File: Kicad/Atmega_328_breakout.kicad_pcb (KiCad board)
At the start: 2 copper layers, 73.8 x 62 mm, 83 parts, among them J1 Power_connector, J10 Device_Connector, J11 Power terminal, J12 Jack-DC, J13 1x2, J14 1x2, J15 1x2, J16 1x2, J17 Conn_01x06, J18 1x2, J19 1x2, J2 ADC_Connector, J20 1x2, J21 1x2, J22 1x2, J23 1x2, J24 1x2, J25 1x2, J26 1x2, J27 1x2, J28 1x2, J29 1x2, J3 Com_header, J30 Pin out, J4 PORB++_connector, J5 PORD_connector, J6 USB, J7 Conn_01x01, Q1 PMOS, SW1 SW_Push, SW2 SW_Push, U1 MCP1700-33, U2 TL071, U3 ATMEGA328P-AU, U4 L7805, U5 MCP2221, U6 NCP1117-5, Y1 Crystal

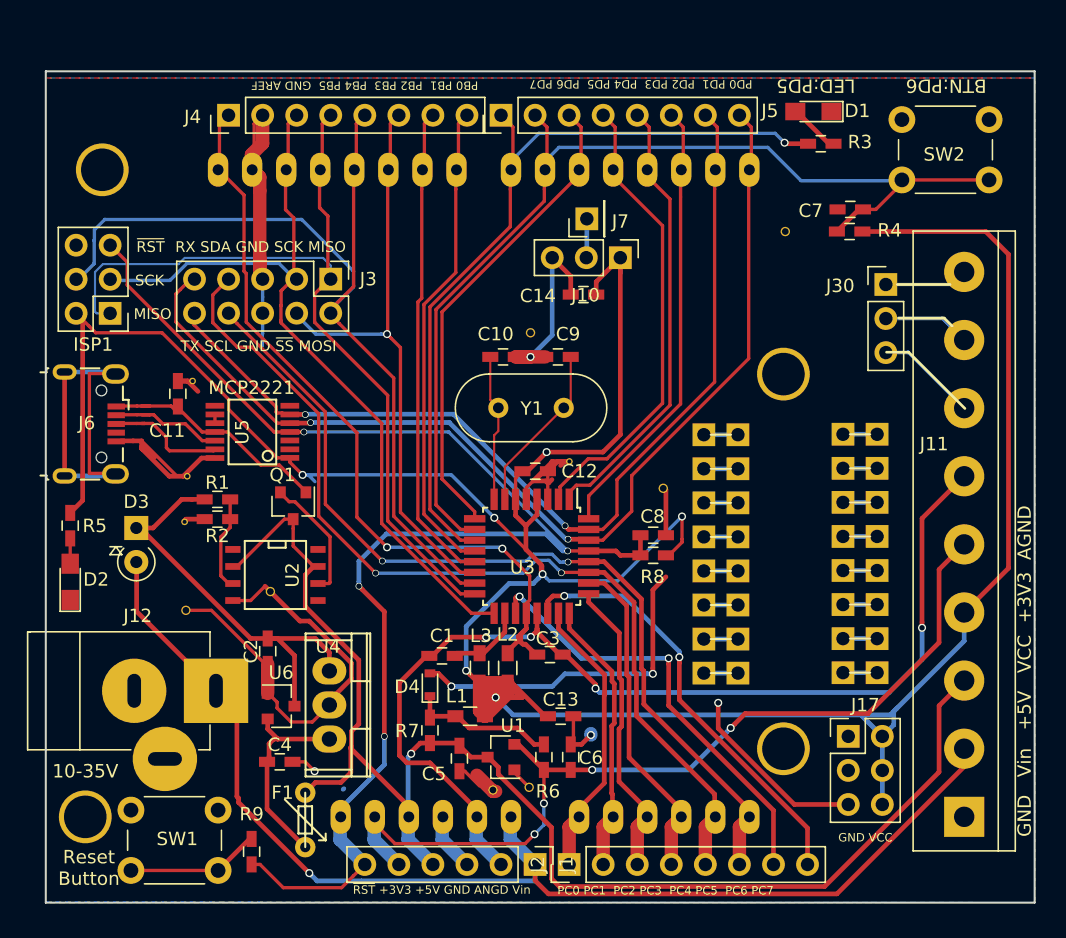
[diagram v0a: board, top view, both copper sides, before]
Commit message: fixed it for kicad 5
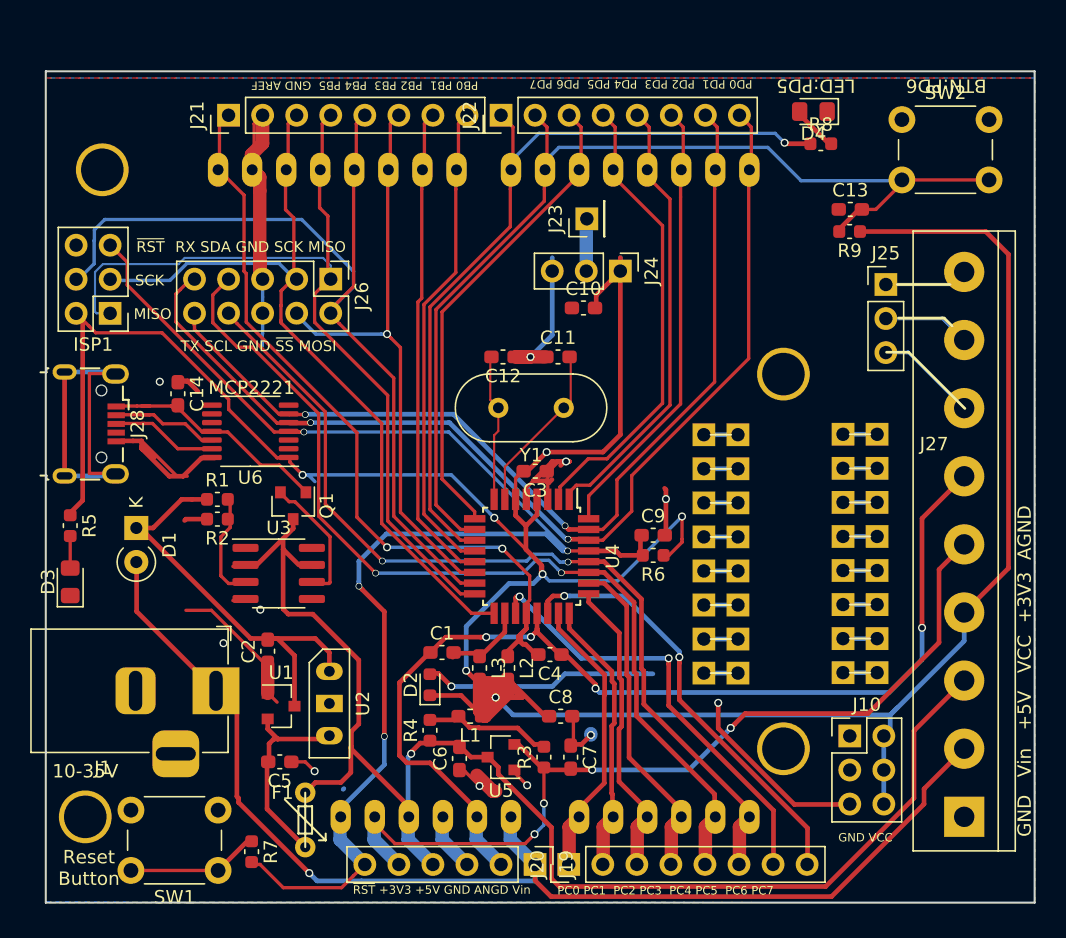
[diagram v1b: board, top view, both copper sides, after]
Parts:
- removed G***: LOGO, jorgen:LOGO
- removed GND (x6), REF**: VIA_GND, jorgen:VIA_GND_0,5
- removed GND (x3), REF**: VIA_GND, jorgen:VIA_GND_0,3
- removed the J17 at (110.1, 103.6)
- removed the J2 at (89.3, 113.2)
- removed the R7 at (78.9, 103.2)
- added J10: Conn_01x06, Connector_PinHeader_2.54mm:PinHeader_2x03_P2.54mm_Vertical, F.Cu at (110.2, 103.6)
- added J20: ADC_Connector, Connector_PinHeader_2.54mm:PinHeader_1x08_P2.54mm_Vertical, F.Cu at (89.2, 113.2)
- added R4: 0R, Capacitor_SMD:C_0603_1608Metric, F.Cu at (78.9, 103.2)
- C1, C2: footprint Capacitors_SMD:C_0603_HandSoldering -> Capacitor_SMD:C_0603_1608Metric_Pad1.08x0.95mm_HandSolder
- C10: renamed from C14; footprint Capacitors_SMD:C_0603_HandSoldering -> Capacitor_SMD:C_0603_1608Metric_Pad1.08x0.95mm_HandSolder
- C11: renamed from C9; footprint Capacitors_SMD:C_0603_HandSoldering -> Capacitor_SMD:C_0603_1608Metric_Pad1.08x0.95mm_HandSolder
- C12: renamed from C10; footprint Capacitors_SMD:C_0603_HandSoldering -> Capacitor_SMD:C_0603_1608Metric_Pad1.08x0.95mm_HandSolder
- C13: renamed from C7; footprint Capacitors_SMD:C_0603_HandSoldering -> Capacitor_SMD:C_0603_1608Metric_Pad1.08x0.95mm_HandSolder
- C14: renamed from C11; footprint Capacitors_SMD:C_0603_HandSoldering -> Capacitor_SMD:C_0603_1608Metric_Pad1.08x0.95mm_HandSolder
- C3: renamed from C12; footprint Capacitors_SMD:C_0603_HandSoldering -> Capacitor_SMD:C_0603_1608Metric_Pad1.08x0.95mm_HandSolder
- C4: renamed from C3; footprint Capacitors_SMD:C_0603_HandSoldering -> Capacitor_SMD:C_0603_1608Metric_Pad1.08x0.95mm_HandSolder
- C5: renamed from C4; footprint Capacitors_SMD:C_0603_HandSoldering -> Capacitor_SMD:C_0603_1608Metric_Pad1.08x0.95mm_HandSolder
- C6: renamed from C5; footprint Capacitors_SMD:C_0603_HandSoldering -> Capacitor_SMD:C_0603_1608Metric_Pad1.08x0.95mm_HandSolder
- C7: renamed from C6; footprint Capacitors_SMD:C_0603_HandSoldering -> Capacitor_SMD:C_0603_1608Metric_Pad1.08x0.95mm_HandSolder
- C8: renamed from C13; footprint Capacitors_SMD:C_0603_HandSoldering -> Capacitor_SMD:C_0603_1608Metric_Pad1.08x0.95mm_HandSolder
- C9: renamed from C8; footprint Capacitors_SMD:C_0603_HandSoldering -> Capacitor_SMD:C_0603_1608Metric_Pad1.08x0.95mm_HandSolder
- D1: renamed from D3; footprint Diodes_THT:D_A-405_P2.54mm_Vertical_KathodeUp -> Diode_THT:D_A-405_P2.54mm_Vertical_KathodeUp
- D2: renamed from D4; footprint Diodes_SMD:D_0603 -> Diode_SMD:D_0603_1608Metric
- D3: renamed from D2; footprint LEDs:LED_0805_HandSoldering -> LED_SMD:LED_0805_2012Metric_Pad1.15x1.40mm_HandSolder
- D4: renamed from D1; footprint LEDs:LED_0805_HandSoldering -> LED_SMD:LED_0805_2012Metric_Pad1.15x1.40mm_HandSolder
- ISP1: footprint Pin_Headers:Pin_Header_Straight_2x03_Pitch2.54mm -> Connector_PinHeader_2.54mm:PinHeader_2x03_P2.54mm_Vertical
- J1: renamed from J12; footprint Connectors:JACK_ALIM -> Connector_BarrelJack:BarrelJack_Horizontal
- J19: renamed from J1; footprint Socket_Strips:Socket_Strip_Straight_1x06_Pitch2.54mm -> Connector_PinHeader_2.54mm:PinHeader_1x06_P2.54mm_Vertical
- J21: renamed from J4; footprint Socket_Strips:Socket_Strip_Straight_1x08_Pitch2.54mm -> Connector_PinHeader_2.54mm:PinHeader_1x08_P2.54mm_Vertical
- J22: renamed from J5; footprint Socket_Strips:Socket_Strip_Straight_1x08_Pitch2.54mm -> Connector_PinHeader_2.54mm:PinHeader_1x08_P2.54mm_Vertical
- J23: renamed from J7; footprint Pin_Headers:Pin_Header_Straight_1x01_Pitch2.54mm -> Connector_PinHeader_2.54mm:PinHeader_1x01_P2.54mm_Vertical
- J24: renamed from J10; footprint Pin_Headers:Pin_Header_Straight_1x03_Pitch2.54mm -> Connector_PinHeader_2.54mm:PinHeader_1x03_P2.54mm_Vertical
- J25: renamed from J30; footprint Pin_Headers:Pin_Header_Straight_1x03_Pitch2.54mm -> Connector_PinHeader_2.54mm:PinHeader_1x03_P2.54mm_Vertical
- J26: renamed from J3; footprint Pin_Headers:Pin_Header_Straight_2x05_Pitch2.54mm -> Connector_PinHeader_2.54mm:PinHeader_2x05_P2.54mm_Vertical
- J28: renamed from J6; footprint Connectors_USB:USB_Micro-B_Wuerth-629105150521 -> Connector_USB:USB_Micro-B_Wuerth_629105150521
- L1, L2, L3: footprint Inductors_SMD:L_0603_HandSoldering -> Inductor_SMD:L_0603_1608Metric_Pad1.05x0.95mm_HandSolder
- Q1: footprint TO_SOT_Packages_SMD:SOT-23 -> Package_TO_SOT_SMD:SOT-23
- R1, R2, R5: footprint Capacitors_SMD:C_0603_HandSoldering -> Capacitor_SMD:C_0603_1608Metric
- R3: renamed from R6; footprint Capacitors_SMD:C_0603_HandSoldering -> Capacitor_SMD:C_0603_1608Metric
- R6: renamed from R8; footprint Capacitors_SMD:C_0603_HandSoldering -> Capacitor_SMD:C_0603_1608Metric
- R7: renamed from R9; footprint Capacitors_SMD:C_0603_HandSoldering -> Capacitor_SMD:C_0603_1608Metric
- R8: renamed from R3; footprint Capacitors_SMD:C_0603_HandSoldering -> Capacitor_SMD:C_0603_1608Metric
- R9: renamed from R4; footprint Capacitors_SMD:C_0603_HandSoldering -> Capacitor_SMD:C_0603_1608Metric
- SW1, SW2: footprint Buttons_Switches_THT:SW_PUSH_6mm_h5mm -> Button_Switch_THT:SW_PUSH_6mm_H5mm
- U1: renamed from U6; footprint TO_SOT_Packages_SMD:SOT-23 -> Package_TO_SOT_SMD:SOT-23
- U2: renamed from U4; footprint Power_Integrations:TO-220 -> jorgen:TO-220-ver2
- U3: renamed from U2; footprint SMD_Packages:SOIC-8-N -> Package_SO:SOIC-8_3.9x4.9mm_P1.27mm
- U4: renamed from U3; footprint Housings_QFP:TQFP-32_7x7mm_Pitch0.8mm -> Package_QFP:TQFP-32_7x7mm_P0.8mm
- U5: renamed from U1; footprint TO_SOT_Packages_SMD:SOT-23 -> Package_TO_SOT_SMD:SOT-23
- U6: renamed from U5; footprint SMD_Packages:SSOP-14 -> Package_SO:TSSOP-14_4.4x5mm_P0.65mm
- Y1: footprint Crystals:Crystal_HC49-U_Vertical -> Crystal:Crystal_HC49-U_Vertical
- moved C10 1.00 mm to (90.3, 71.7)
- moved J24 1.00 mm to (93.1, 68.9)
- moved U3 0.27 mm to (67.6, 91.5), turned to 0 degrees
- moved C1 0.26 mm to (79.8, 97.3)
- moved U6 0.17 mm to (65.5, 80.8), turned to 180 degrees
- moved U2 0.11 mm to (71.4, 101.2)
- renumbered J22 to J11, J23 to J12, J24 to J13, J25 to J14, J26 to J15, J27 to J16, J28 to J17, J29 to J18, J13 to J2, J11 to J27, J14 to J3, J15 to J4, J16 to J5, J18 to J6, J19 to J7, J20 to J8, J21 to J9
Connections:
- net /AGND renamed AGND
- net /MCP_GP0 renamed Net-(U6-Pad2)
- net /MCP_GP1 renamed Net-(U6-Pad3)
- net /MCP_GP2 renamed Net-(U6-Pad7)
- net /MCP_GP3 renamed Net-(U6-Pad8)
- net /PB0 renamed PB0
- net /PB1 renamed PB1
- net /PB2 renamed PB2
- net /PB3 renamed PB3
- net /PB4 renamed PB4
- net /PB5 renamed PB5
- net /PC0 renamed PC0
- net /PC1 renamed PC1
- net /PC2 renamed PC2
- net /PC3 renamed PC3
- net /PC4(SDA) renamed PC4(SDA)
- net /PC5(SCL) renamed PC5(SCL)
- net /PD0(RX) renamed PD0(RX)
- net /PD1(TX) renamed PD1(TX)
- net /PD2 renamed PD2
- net /PD3 renamed PD3
- net /PD4 renamed PD4
- net /PD5 renamed PD5
- net /PD6 renamed PD6
- net /PD7 renamed PD7
- net /V_supply renamed V_supply
- net /Vusb renamed VUSB
- net /XTAL1(PB6) renamed XTAL1(PB6)
- net /XTAL2(PB7) renamed XTAL2(PB7)
- net /~RESET renamed ~RESET
- D2 pad 1: Net-(D4-Pad1) -> VCC
- L1 pad 2: Net-(D4-Pad1) -> Net-(L1-Pad2)
- R3 pad 2: Net-(D4-Pad1) -> Net-(L1-Pad2)
- U4 pad 19: /ADC6 -> ADC6
- U4 pad 22: /ADC7 -> ADC7
- U6 pad 10: /MCP_SCL -> Net-(U6-Pad10)
- U6 pad 9: /MCP_SCL -> Net-(U6-Pad9)
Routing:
- net ADC6: track 0.00 -> 33.1 mm, vias 0 -> 2
- net /ADC6: track 33.1 -> 0.00 mm, vias 2 -> 0
- net ADC7: track 0.00 -> 32.4 mm, vias 0 -> 2
- net /ADC7: track 32.4 -> 0.00 mm, vias 2 -> 0
- net GND: track 166.8 -> 136.7 mm, vias 6 -> 12
- net Net-(D4-Pad1): track 11.0 -> 0.00 mm
- net Net-(L1-Pad2): track 0.00 -> 9.78 mm
- net +5V: track 110.2 -> 112.0 mm
- net VCC: track 250.5 -> 252.3 mm
- net PD1(TX): track 72.9 -> 74.3 mm
- net V_supply: track 94.9 -> 96.3 mm
- net Net-(J23-Pad1): track 2.92 -> 3.92 mm
- net Net-(J28-Pad3): track 8.26 -> 7.47 mm
- net /MCP_SCL: track 0.65 -> 0.00 mm
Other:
- rule trace_min: 0.16 -> 0

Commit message: added available parts from jlcpcb for bom
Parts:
- R1, R2, R4, R6, R7, R8, R9: footprint Capacitor_SMD:C_0603_1608Metric -> Resistor_SMD:R_0603_1608Metric_Pad0.98x0.95mm_HandSolder
- R3: value 0R -> 0.0R; footprint Capacitor_SMD:C_0603_1608Metric -> Resistor_SMD:R_0603_1608Metric_Pad0.98x0.95mm_HandSolder
- R5: value 1kR -> 1k; footprint Capacitor_SMD:C_0603_1608Metric -> Resistor_SMD:R_0603_1608Metric_Pad0.98x0.95mm_HandSolder

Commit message: compiled and packed gerber
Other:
- rule pad_to_mask_clearance: 0.2 -> 0

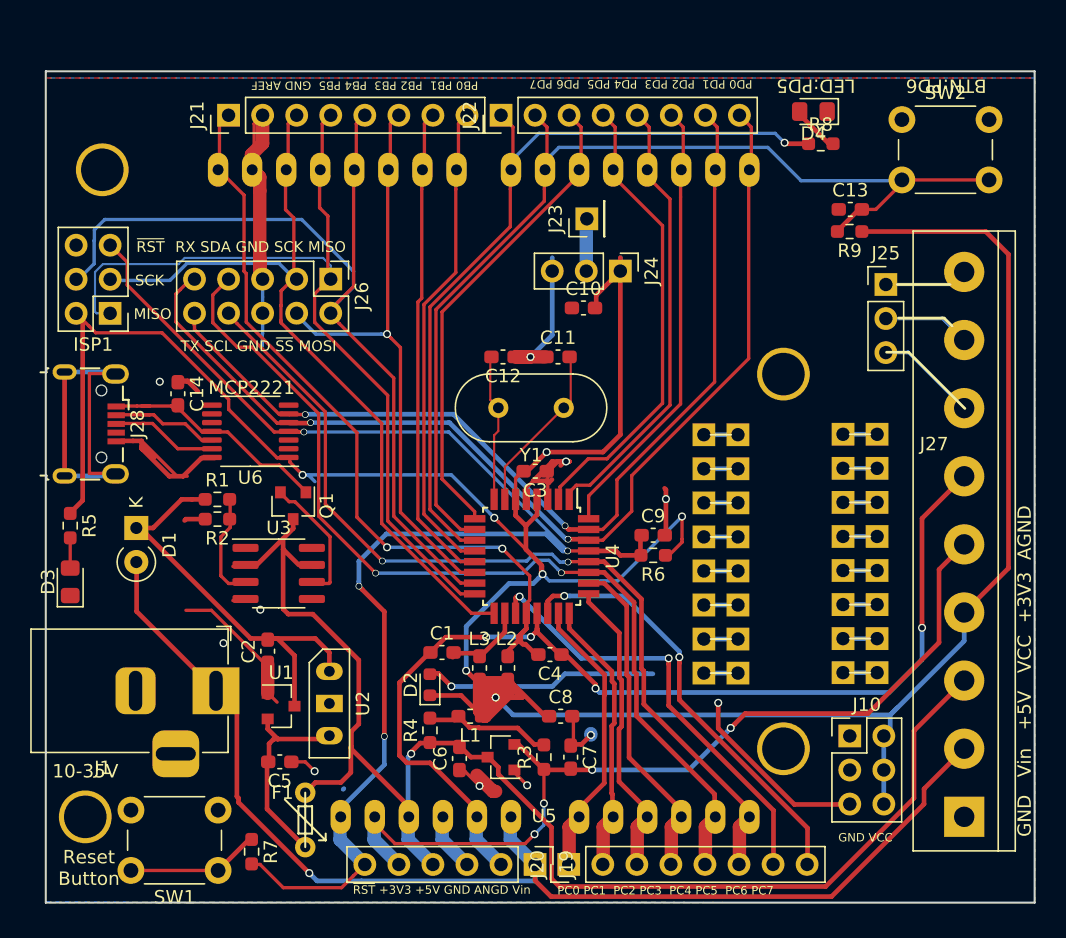
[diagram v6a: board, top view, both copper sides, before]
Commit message: replace as much as possible with smd
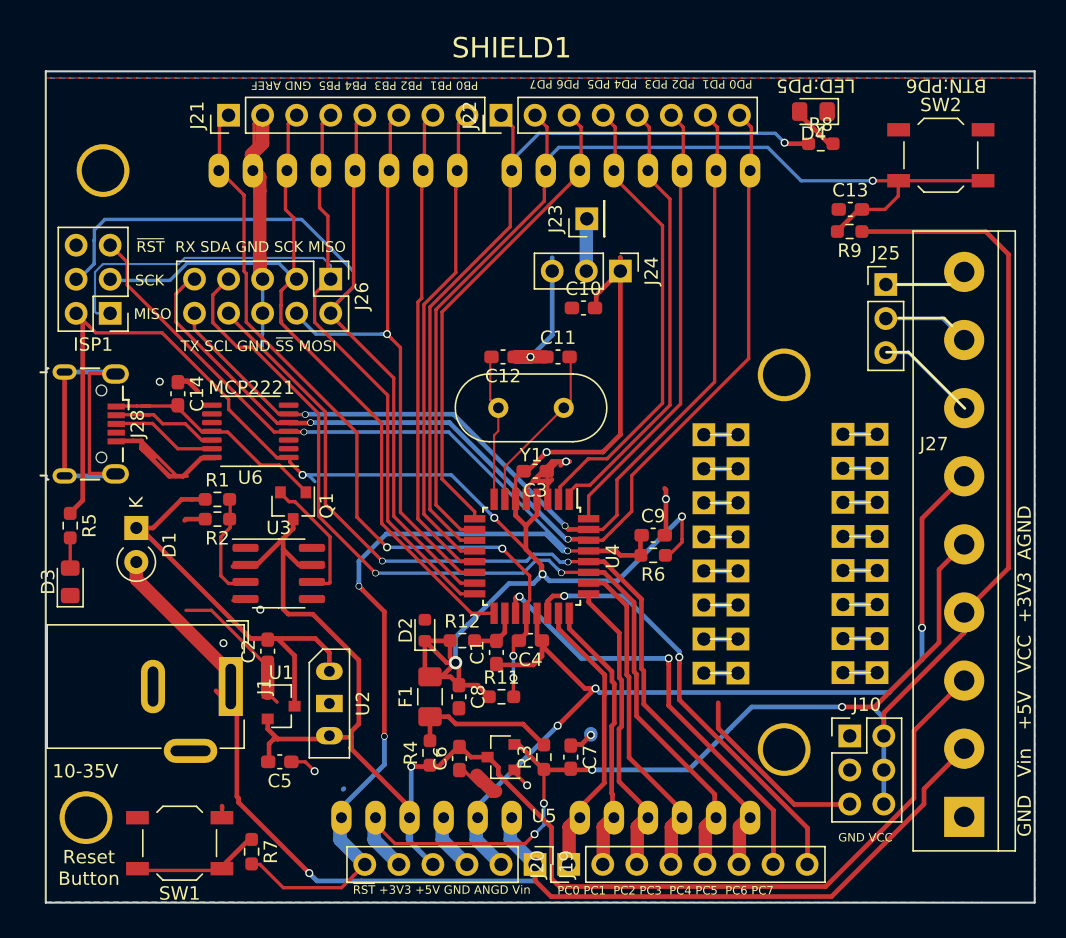
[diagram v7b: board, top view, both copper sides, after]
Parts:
- removed L1, L2, L3: F B, Inductor_SMD:L_0603_1608Metric_Pad1.05x0.95mm_HandSolder
- added R11: 0R, Resistor_SMD:R_0603_1608Metric_Pad0.98x0.95mm_HandSolder, F.Cu at (84.2, 100.6)
- added R12: 0R, Resistor_SMD:R_0603_1608Metric_Pad0.98x0.95mm_HandSolder, F.Cu at (81.3, 96.5)
- F1: footprint jorgen:Polyfuse -> Fuse:Fuse_1206_3216Metric_Pad1.42x1.75mm_HandSolder
- J1: footprint Connector_BarrelJack:BarrelJack_Horizontal -> Connector_BarrelJack:BarrelJack_Wuerth_6941xx301002
- SW1, SW2: footprint Button_Switch_THT:SW_PUSH_6mm_H5mm -> Button_Switch_SMD:SW_SPST_TL3342
- moved F1 13.1 mm to (78.9, 100.6), turned to 90 degrees
- moved C8 7.73 mm to (81.1, 100.6), turned to 270 degrees
- moved D2 4.07 mm to (78.5, 95.7)
- moved C1 4.06 mm to (83.9, 97.3), turned to 90 degrees
- moved SW2 3.94 mm to (117.0, 60.3)
- moved SW1 3.51 mm to (60.2, 111.6)
- moved C4 1.79 mm to (86.4, 96.5)
- moved R4 1.69 mm to (78.9, 104.8)
- moved J1 1.15 mm to (64.0, 99.9), turned to 270 degrees
- moved SHIELD1 0.08 mm to (50.5, 115.8)
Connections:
- C5 pad 2: Net-(C5-Pad2) -> +5V
- F1 pad 1: +5V -> Net-(F1-Pad1)
- F1 pad 2: Net-(C5-Pad2) -> VCC
- R3 pad 2: Net-(L1-Pad2) -> Net-(F1-Pad1)
- R4 pad 2: Net-(L1-Pad2) -> Net-(F1-Pad1)
- U1 pad 2: Net-(C5-Pad2) -> +5V
- U2 pad 3: Net-(C5-Pad2) -> +5V
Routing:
- net VCC: track 252.3 -> 202.2 mm, vias 7 -> 6
- net GND: track 136.7 -> 117.4 mm, vias 12 -> 9
- net Net-(C5-Pad2): track 15.2 -> 0.00 mm
- net Net-(F1-Pad1): track 0.00 -> 11.2 mm
- net Net-(L1-Pad2): track 9.78 -> 0.00 mm
- net AGND: track 82.1 -> 75.8 mm, vias 4 -> 3
- net +5V: track 112.0 -> 114.9 mm
- net AVCC: track 6.06 -> 4.06 mm
- net AREF: track 58.4 -> 58.9 mm, vias 2 -> 4
- net PD6: track 79.2 -> 78.8 mm, vias 0 -> 1

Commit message: All parts added and part number
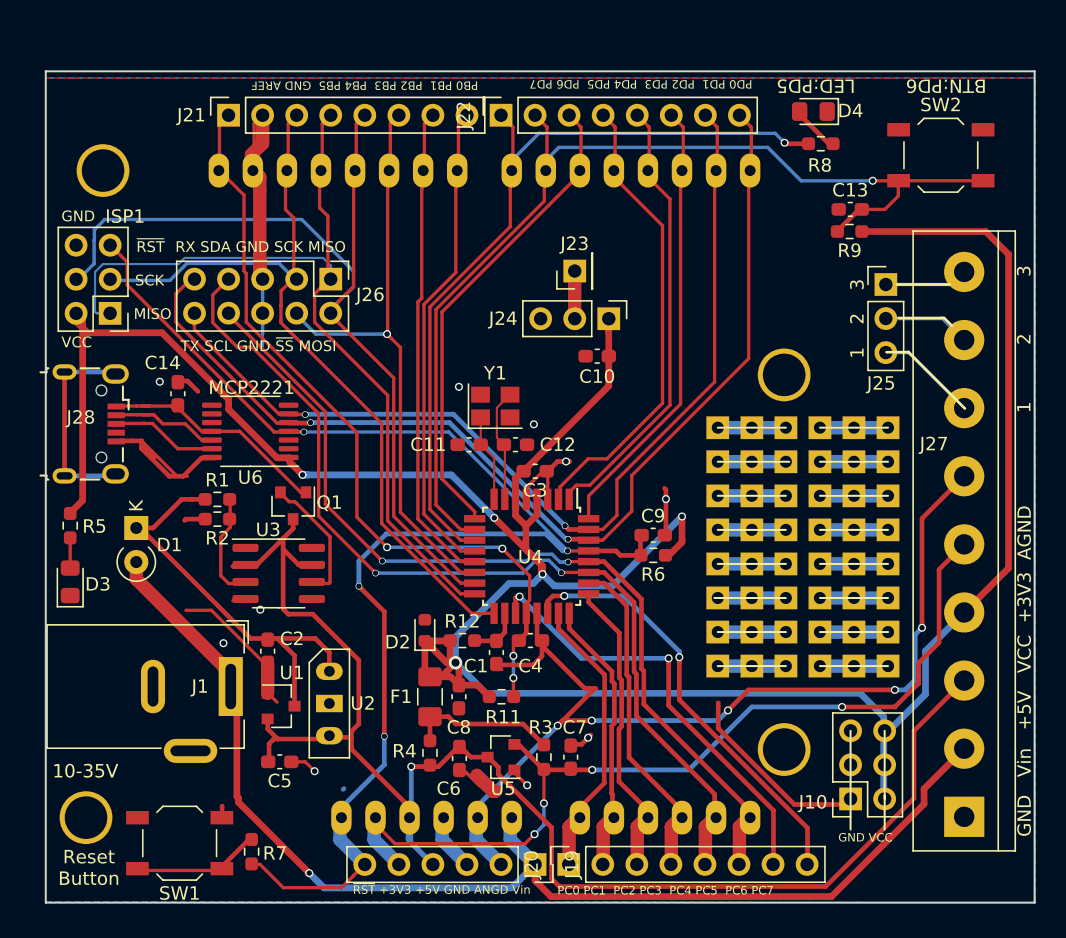
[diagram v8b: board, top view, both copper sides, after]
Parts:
- J10: footprint Connector_PinHeader_2.54mm:PinHeader_2x03_P2.54mm_Vertical -> Connector_PinSocket_2.54mm:PinSocket_2x03_P2.54mm_Vertical
- J11, J12, J13, J14, J15, J16, J17, J18, J2, J3, J4, J5, J6, J7, J8, J9: value 1x2 -> 01x03; footprint jorgen:Pin_Header_Straight_1x02_Pitch2.54mm -> jorgen:conn_01x03_square
- J19: footprint Connector_PinHeader_2.54mm:PinHeader_1x06_P2.54mm_Vertical -> Connector_PinSocket_2.54mm:PinSocket_1x06_P2.54mm_Vertical
- J20, J21, J22: footprint Connector_PinHeader_2.54mm:PinHeader_1x08_P2.54mm_Vertical -> Connector_PinSocket_2.54mm:PinSocket_1x08_P2.54mm_Vertical
- Y1: value Crystal -> Crystal_GND24; footprint Crystal:Crystal_HC49-U_Vertical -> Crystal:Crystal_SMD_3225-4Pin_3.2x2.5mm
- moved J3 20.2 mm to (104.2, 76.8), turned to 0 degrees
- moved J2 19.7 mm to (111.8, 76.8), turned to 0 degrees
- moved J6 17.3 mm to (111.8, 81.8), turned to 0 degrees
- moved J5 15.5 mm to (104.2, 79.3), turned to 0 degrees
- moved J12 13.8 mm to (111.8, 86.9), turned to 0 degrees
- moved J8 13.2 mm to (111.8, 84.4), turned to 0 degrees
- moved J4 12.1 mm to (111.8, 79.3), turned to 0 degrees
- moved J7 10.6 mm to (104.2, 81.8), turned to 0 degrees
- moved J13 10.1 mm to (104.2, 89.5), turned to 0 degrees
- moved J17 10.1 mm to (104.2, 94.5), turned to 0 degrees
- moved J14 9.61 mm to (111.8, 89.5), turned to 0 degrees
- moved C11 9.32 mm to (81.8, 81.8)
- moved J16 8.65 mm to (111.8, 92.0), turned to 0 degrees
- moved J15 8.41 mm to (104.2, 92.0), turned to 0 degrees
- moved C12 6.62 mm to (85.3, 81.8)
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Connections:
- C11 pad 2: XTAL1(PB6) -> XTAL2(PB7)
- C12 pad 2: XTAL2(PB7) -> XTAL1(PB6)
- Y1 pad 1: XTAL1(PB6) -> XTAL2(PB7)
- Y1 pad 2: XTAL2(PB7) -> GND
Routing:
- net VCC: track 202.2 -> 224.9 mm, vias 6 -> 5
- net GND: track 117.4 -> 98.8 mm, vias 9 -> 10
- net Net-(J28-Pad6): track 28.1 -> 15.5 mm
- net V_supply: track 96.4 -> 87.8 mm
- net XTAL2(PB7): track 11.0 -> 6.52 mm
- net AGND: track 75.8 -> 80.1 mm, vias 3 -> 5
- net XTAL1(PB6): track 12.7 -> 8.45 mm
- net Net-(J9-Pad1): track 2.54 -> 5.08 mm
- net Net-(J8-Pad1): track 2.54 -> 5.08 mm
- net Net-(J7-Pad1): track 2.54 -> 5.08 mm
- net Net-(J6-Pad1): track 2.54 -> 5.08 mm
- net Net-(J5-Pad1): track 2.54 -> 5.08 mm
- net Net-(J4-Pad1): track 2.54 -> 5.08 mm
- net Net-(J3-Pad1): track 2.54 -> 5.08 mm
- net Net-(J2-Pad1): track 2.54 -> 5.08 mm
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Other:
- board text added: "1"
- board text added: "2"
- board text added: "3"
- board text added: "GND"
- board text added: "VCC"
